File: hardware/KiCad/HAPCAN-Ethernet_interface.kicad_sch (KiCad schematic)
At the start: 95 parts, among them CON1 Connectors CAN bus, IC1 LMR51430Y, IC2 MCP2561-E-SN, IC3 TLV62568DBV, IC4 STM32F072C8Tx, IC5 MCP3422A0-E/MS, IC6 USBLC6-2SC6, IC7 FT230XS, IC8 BQ32000, T1 DMC2053UVT, U1 HLK-7628N

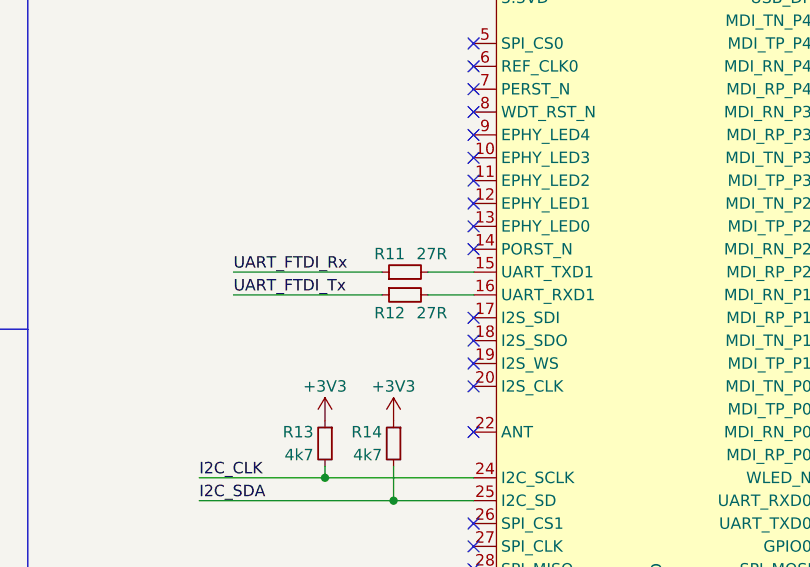
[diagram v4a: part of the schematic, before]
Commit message: Added DNP flag to UART1 resistors (collided connection to UART0)
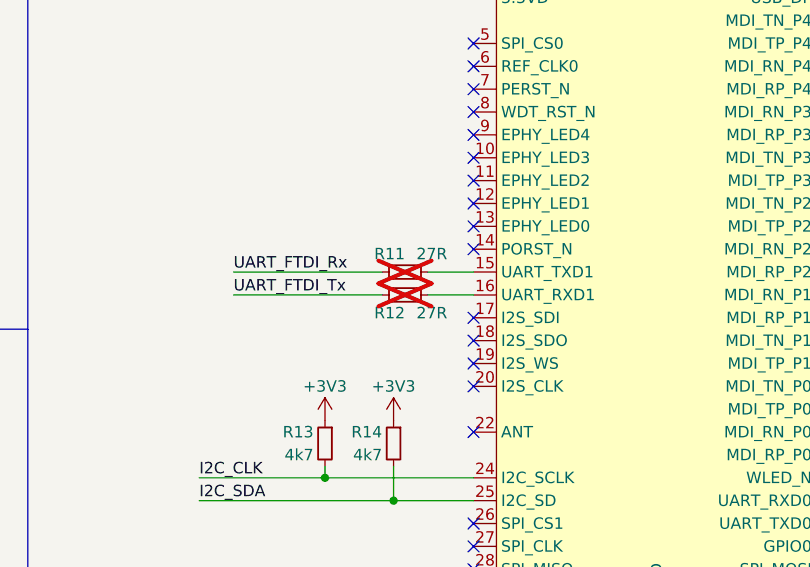
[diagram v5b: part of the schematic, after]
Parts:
- L2: Note (none) -> Populated IHLP2525CZER1R5M01 on the first prototype
- R11, R12: now not fitted; now left out of the parts list
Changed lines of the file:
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@@
 		(unit 1)
 		(exclude_from_sim no)
-		(in_bom yes)
-		(on_board yes)
-		(dnp no)
+		(in_bom no)
+		(on_board yes)
+		(dnp yes)
 		(property "Reference" "R12"
 			(at 201.93 132.08 90)
@@
 		)
 		(property "Description" "Resistor, small symbol"
+			(at 201.93 130.81 0)
+			(effects
+				(font
+					(size 1.27 1.27)
+				)
+				(hide yes)
+			)
+		)
+		(property "eshop" ""
 			(at 201.93 130.81 0)
 			(effects
@@
 		(unit 1)
 		(exclude_from_sim no)
-		(in_bom yes)
-		(on_board yes)
-		(dnp no)
+		(in_bom no)
+		(on_board yes)
+		(dnp yes)
 		(property "Reference" "R11"
 			(at 201.93 127 90)
@@
 		)
 		(property "Description" "Resistor, small symbol"
+			(at 201.93 128.27 0)
+			(effects
+				(font
+					(size 1.27 1.27)
+				)
+				(hide yes)
+			)
+		)
+		(property "eshop" ""
 			(at 201.93 128.27 0)
 			(effects
@@
 			(effects
 				(font
+					(size 1.27 1.27)
+				)
+				(hide yes)
+			)
+		)
+		(property "eshop" ""
+			(at 351.79 34.29 0)
+			(effects
+				(font
+					(size 1.27 1.27)
+				)
+				(hide yes)
+			)
+		)
+		(property "Note" "Populated IHLP2525CZER1R5M01 on the first prototype"
+			(at 351.79 34.29 90)
+			(effects
+				(font

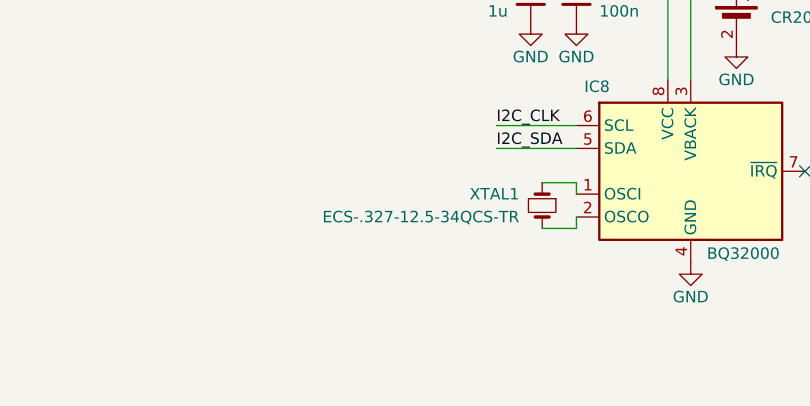
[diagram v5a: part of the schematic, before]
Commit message: Added note about crystal load capacitors
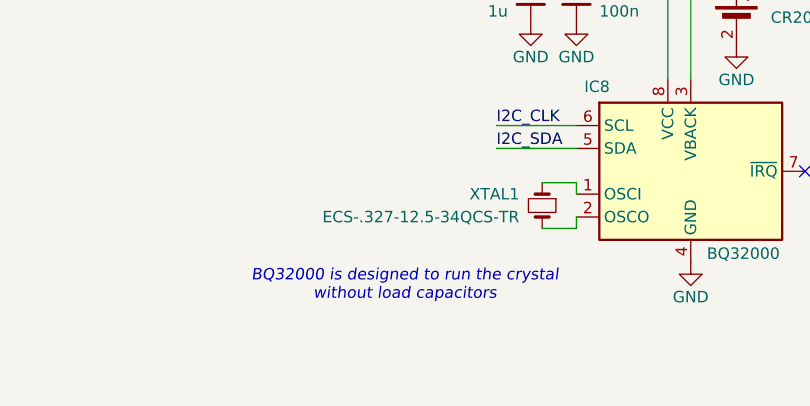
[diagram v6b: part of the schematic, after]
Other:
- note added: "BQ32000 is designed to run the crystal without load capacitors"
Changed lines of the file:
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@@
+		)
+	)
+	(text "BQ32000 is designed to run the crystal\nwithout load capacitors"
+		(exclude_from_sim no)
+		(at 57.15 273.05 0)
+		(effects
+			(font
+				(size 1.27 1.27)
+				(italic yes)
+			)
 		)
 	)

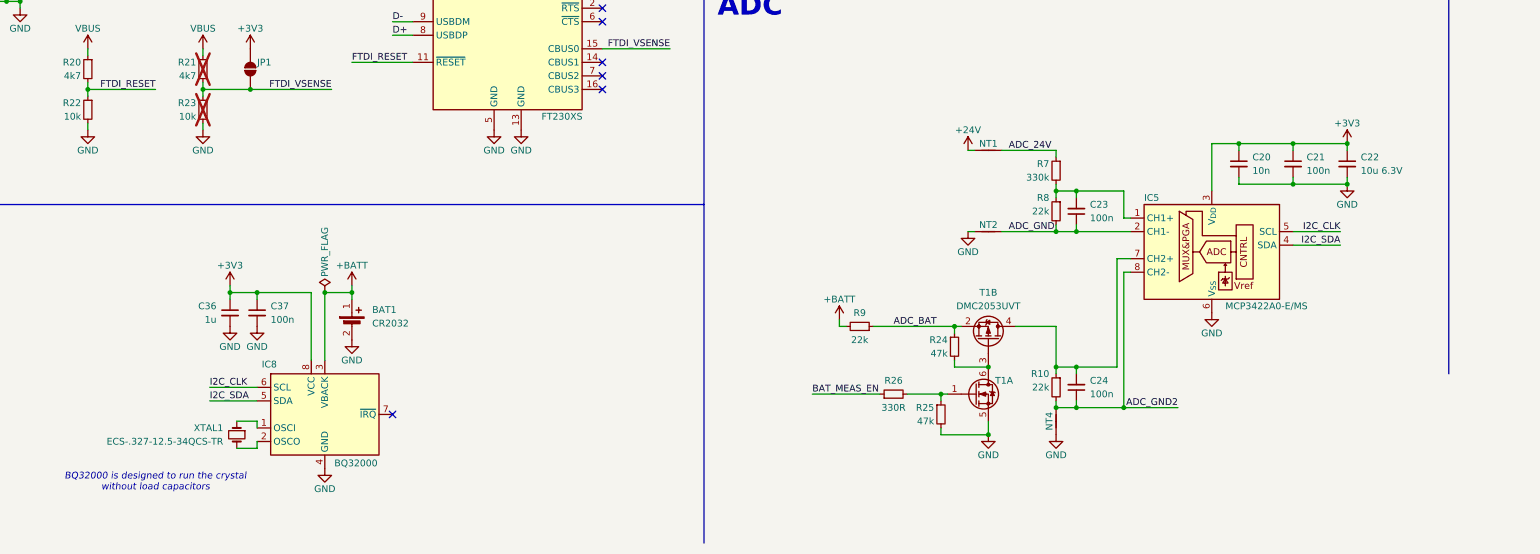
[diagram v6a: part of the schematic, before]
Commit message: Fixed a resistor value near the ADC, added some notes to the schematic
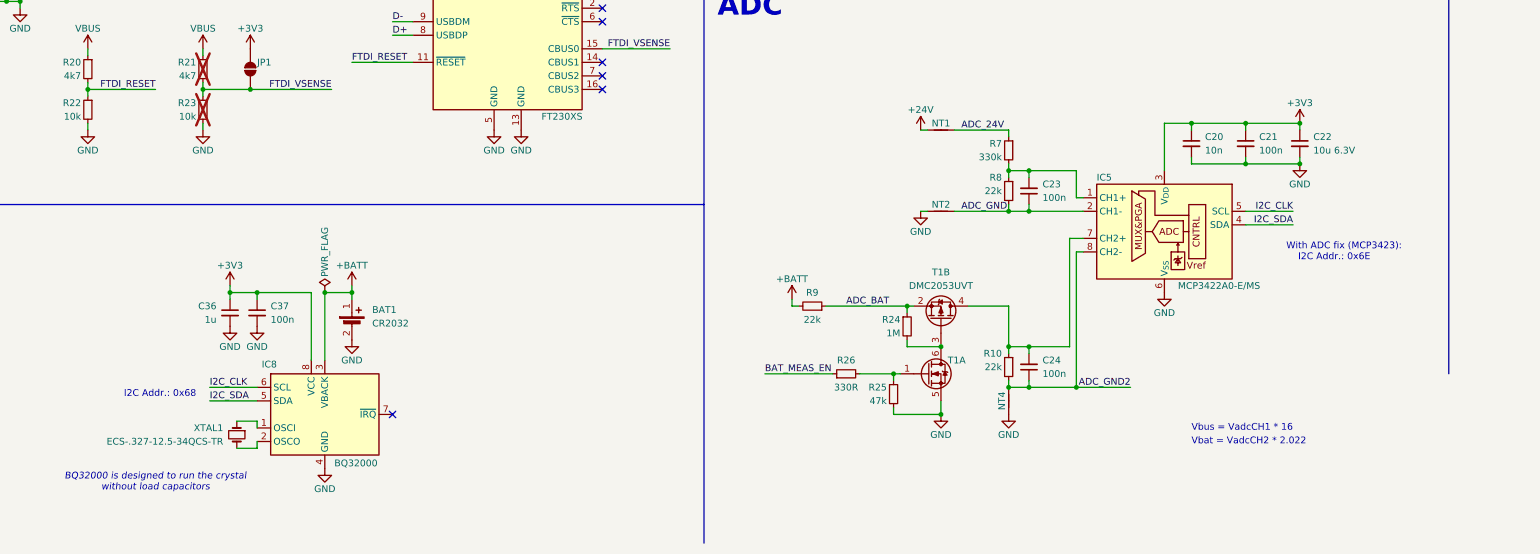
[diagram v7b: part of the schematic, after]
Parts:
- R24: value 47k -> 1M
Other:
- note added: "I2C Addr.: 0x68"
- note added: "Vbat = VadcCH2 * 2.022"
- note added: "Vbus = VadcCH1 * 16"
- note added: "With ADC fix (MCP3423): I2C Addr.: 0x6E"
- moved on the sheet: C20, C21, C22, C23, C24, IC5, NT1, NT2, NT4, R10, R24, R25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
